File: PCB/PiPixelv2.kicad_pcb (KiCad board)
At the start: 2 copper layers, 65 x 30 mm, 13 parts, among them J1 Raspberry_Pi_2_3, J2 Barrel_Jack_Switch, J3 Conn_01x02, J4 Conn_01x04, U1 74AHC125

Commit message: Modified Pi Header to show on BSilk
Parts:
- J1: footprint Pin_Headers:Pin_Header_Straight_2x20_Pitch2.54mm -> BSilk_PiHeader:Pin_Header_Straight_2x20_Pitch2.54mm

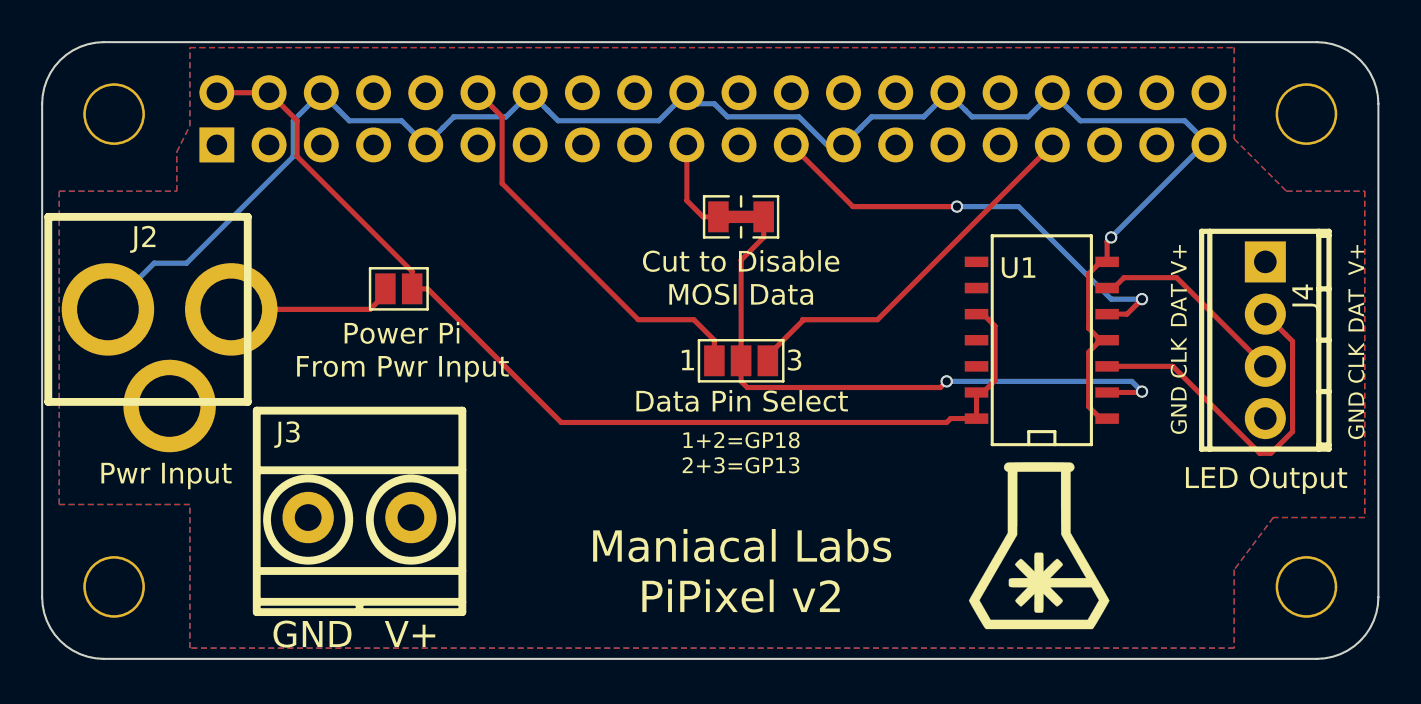
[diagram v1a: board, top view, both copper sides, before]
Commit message: Changed v2 design to TH Level Shifter
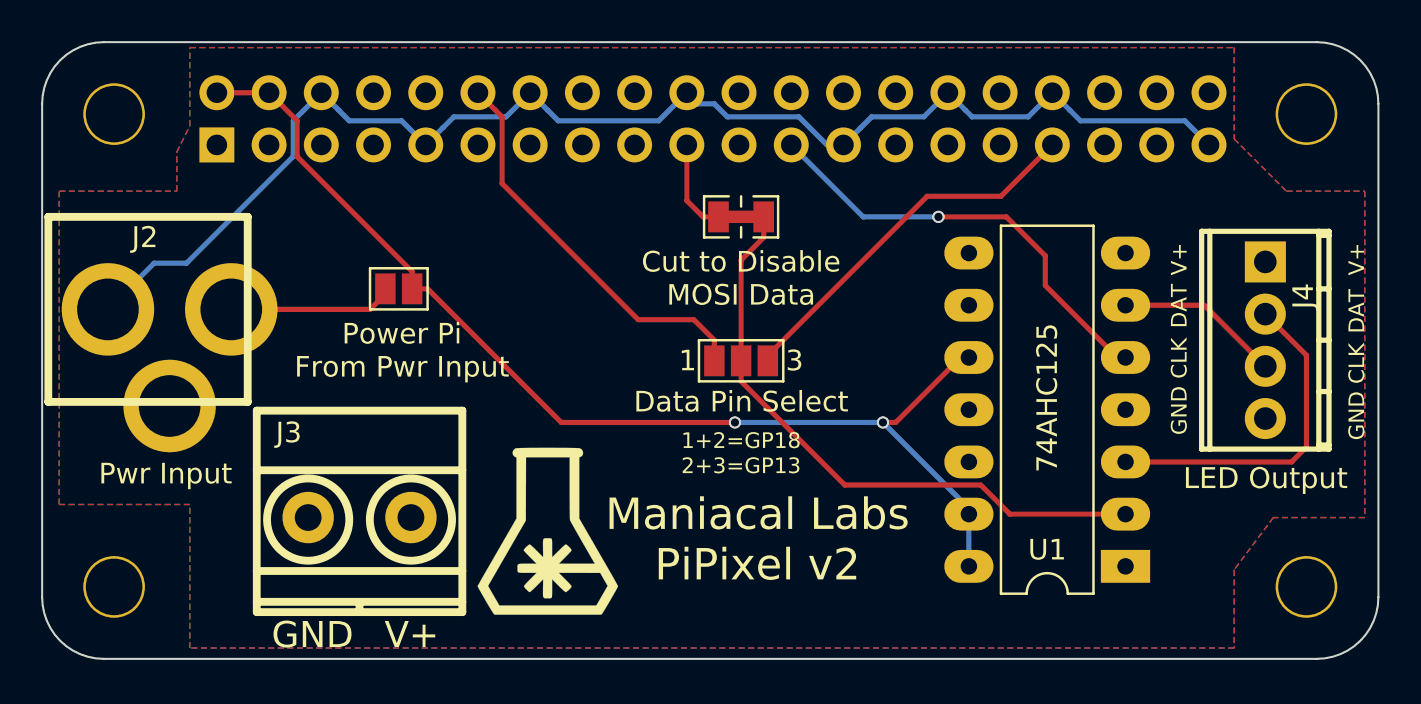
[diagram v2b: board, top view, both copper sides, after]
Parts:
- U1: footprint SMD_Packages:SOIC-14_N -> Housings_DIP:DIP-14_W7.62mm_LongPads
- moved G*** 23.9 mm to (37.1, 48.3)
- moved U1 11.8 mm to (65.2, 50.0), turned to 180 degrees
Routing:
- net GND: track 83.7 -> 66.6 mm, vias 1 -> 0
- net 5V: track 51.4 -> 54.8 mm, vias 0 -> 2
- net Net-(J4-Pad3): track 9.69 -> 8.03 mm
- net Net-(J4-Pad2): track 17.5 -> 16.4 mm
- net CLK: track 22.2 -> 21.4 mm, vias 2 -> 1
- net LS_IN: track 30.1 -> 29.8 mm, vias 2 -> 0
